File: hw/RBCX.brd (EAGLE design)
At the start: 100 x 100 mm, 463 parts, among them IC1 AMS1117-3.3, IC10 INA180A4, IC11 INA180A4, IC12 MPU-6050, IC13 STM32F103VCT6, IC2 DRV8833PWP, IC3 INA180A4, IC4 INA180A4, IC5 DRV8833PWP, IC6 INA180A4, IC7 INA180A4, IC8 INA180A4, IC9 INA180A4, P1 M1, P2 M2, P3 M3, P4 M4, Q1 NCE20P45Q, Q10 2N7002, Q2 NCE20P45Q, Q3 2N7002, Q4 2N7002, Q5 2N7002, Q6 2N7002, Q7 2N7002, Q8 2N7002, Q9 2N7002, X1 POWER_IN, X2 POWER_OUT, X3 52559-3092, X4 uUSB, Y1 5032/2P, Y2 3215_2P

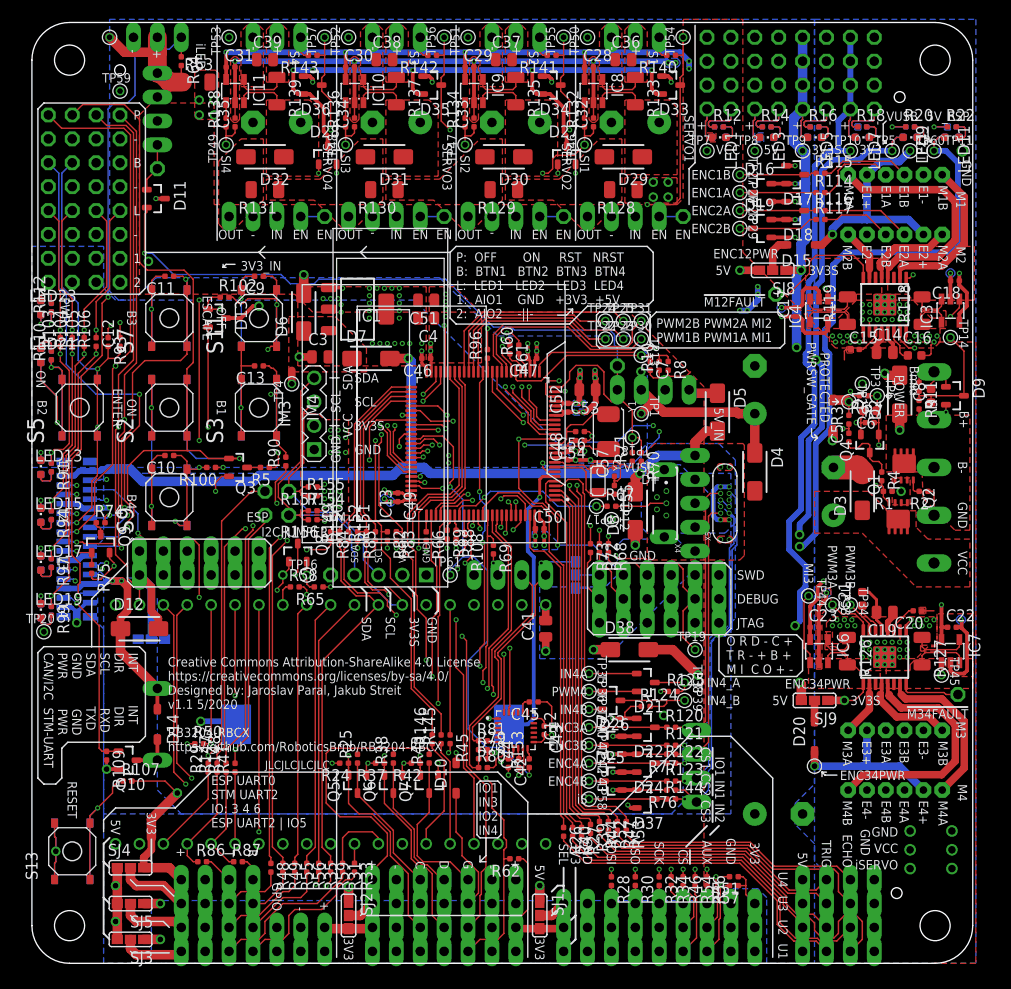
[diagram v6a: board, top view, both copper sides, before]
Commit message: hw: update and fix silkscreens
- fix position of labels
- add testpoint labels
- improve groups of text (separate columns in text labels)
- add label for capacitors polarity
- change layer from `tDocu` to `Document` for label in library `switch-omron.lbr`
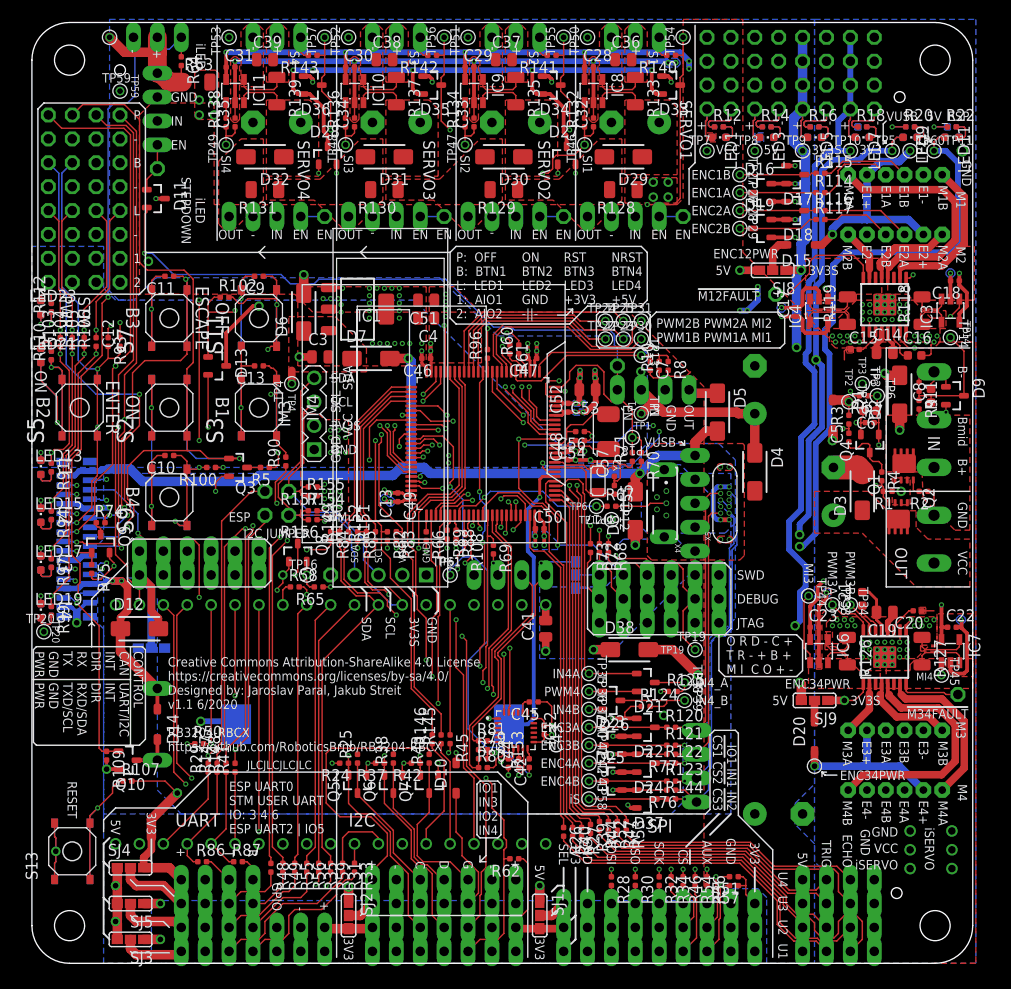
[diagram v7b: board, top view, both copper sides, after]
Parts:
- moved D13 5.08 mm to (19.7, 63.5)
- moved SJ7 0.95 mm to (12.7, 33.5)
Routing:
- net ESP_EN: track 177.6 -> 172.5 mm
- net BUTTON_OFF: track 33.1 -> 38.1 mm
- net +3V3S: track 567.6 -> 571.8 mm
- net EXPANDER_COM_PWR: track 30.0 -> 30.9 mm
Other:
- board text added: "BUZ"
- board text added: "CC1"
- board text added: "CC2"
- board text added: "CONTROL CAN INT DIR RX TX GND PWR"
- board text added: "Creative Commons Attribution-ShareAlike 4.0 License https://creativecommons.org/licenses/by-sa/4.0/ Designed by: Jaroslav Paral, Jakub Streit v1.1 6/2020 RB3204-RBCX https://github.com/RoboticsBrno/RB3204-RBCX"
- board text added: "DM"
- board text added: "ESP UART0 STM USER UART IO: 3 4 6 ESP UART2 | IO5"
- board text added: "ESP UART0 STM USER UART IO: 6 4 3 IO5 | ESP UART2"
- board text added: "MAIN POWERSUPPLY"
- board text added: "MI4"
- board text added: "NRST BTN4 LED4 +5V"
- board text added: "OFF BTN1 LED1 AIO1 AIO2"
- board text added: "ON BTN2 LED2 GND -||-"
- board text added: "ON BTN2 LED2 GND GND"
- board text added: "P: NRST B: BTN4 L: LED4 1: +5V 2: +5V"
- board text added: "P: OFF B: BTN1 L: LED1 1: AIO1 2: AIO2"
- board text added: "RB3204-RBCX v1.1 6/2020 CC-SA 4.0 https://github.com/ RoboticsBrno/ RB3204-RBCX"
- board text added: "RST BTN3 LED3 +3V3"
- board text added: "RST BTN3 LED3 +3V3 +3V3"
- board text added: "SBU1"
- board text added: "SBU2"
- board text added: "STM PWR"
- board text added: "TP1"
- board text added: "TP12"
- board text added: "TP13(V_BAT)"
- board text added: "TP14"
- board text added: "TP16"
- board text added: "TP18"
- board text added: "TP19"
- board text added: "TP2"
- board text added: "TP20"
- board text added: "TP3"
- board text added: "TP4"
- board text added: "TP59"
- board text added: "TP6"
- board text added: "TP61"
- board text added: "UART /I2C INT DIR RXD /SDA TXD /SCL GND PWR"
- board text added: "UART/I2C INT DIR RXD/SDA TXD/SCL GND PWR"
- board text added: "V_BAT/2"
- board text added: "iLED STEPDOWN"
- board text removed: "3V3_IN"
- board text removed: "5V_IN"
- board text removed: "CAN/I2C STM-UART PWR PWR GND GND SDA TXD SCL RXD DIR DIR INT INT"
- board text removed: "Creative Commons Attribution-ShareAlike 4.0 License https://creativecommons.org/licenses/by-sa/4.0/ Designed by: Jaroslav Paral, Jakub Streit v1.1 5/2020 RB3204-RBCX https://github.com/RoboticsBrno/RB3204-RBCX"
- board text removed: "D+"
- board text removed: "D-"
- board text removed: "ESP UART0 STM UART2 IO: 3 4 6 ESP UART2 | IO5"
- board text removed: "ESP UART0 STM UART2 IO: 6 4 3 IO5 | ESP UART2"
- board text removed: "INT INT DIR DIR SCL RXD SDA TXD GND GND PWR PWR CAN/I2C STM-UART"
- board text removed: "P: NRST RST ON OFF B: BTN4 BTN3 BTN2 BTN1 L: LED4 LED3 LED2 LED1 1: +5V +3V3 GND AIO1 2: +5V +3V3 GND AIO2"
- board text removed: "P: OFF ON RST NRST B: BTN1 BTN2 BTN3 BTN4 L: LED1 LED2 LED3 LED4 1: AIO1 GND +3V3 +5V 2: AIO2 -||-"
- board text removed: "POWER"
- board text removed: "PROTECTED"
- board text removed: "PWR"
- board text removed: "PWRSW_GATE"
- board text removed: "RB3204-RBCX v1.1 5/2020 https://github.com/ RoboticsBrno/RB3204-RBCX CC-SA 4.0"

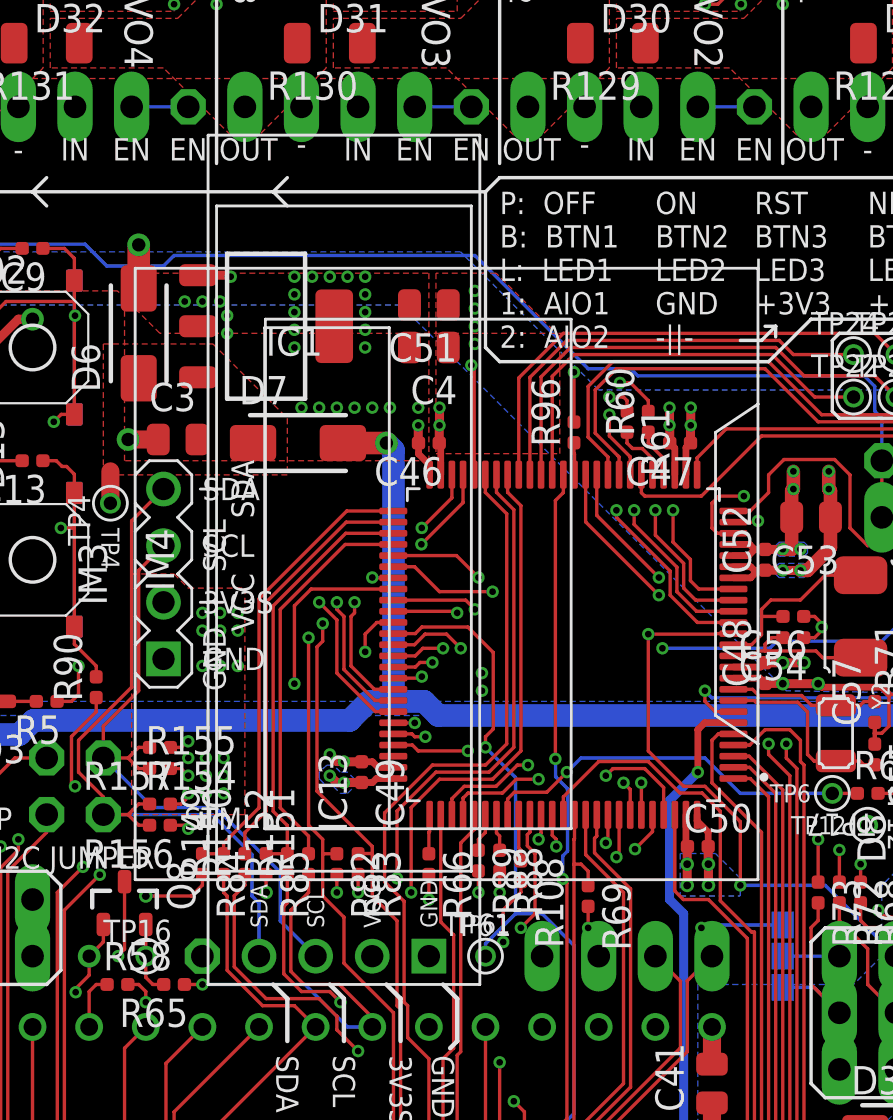
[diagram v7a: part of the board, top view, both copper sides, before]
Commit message: hw: change outline layer of display modules
- `diy-modules.lbr` - change outline layer from `tPlace` to `Document`
  - footprint `DISPLAY-OLED-128X32`
  - footprint `DISPLAY-OLED-128X64-I2C_W-HOLES`
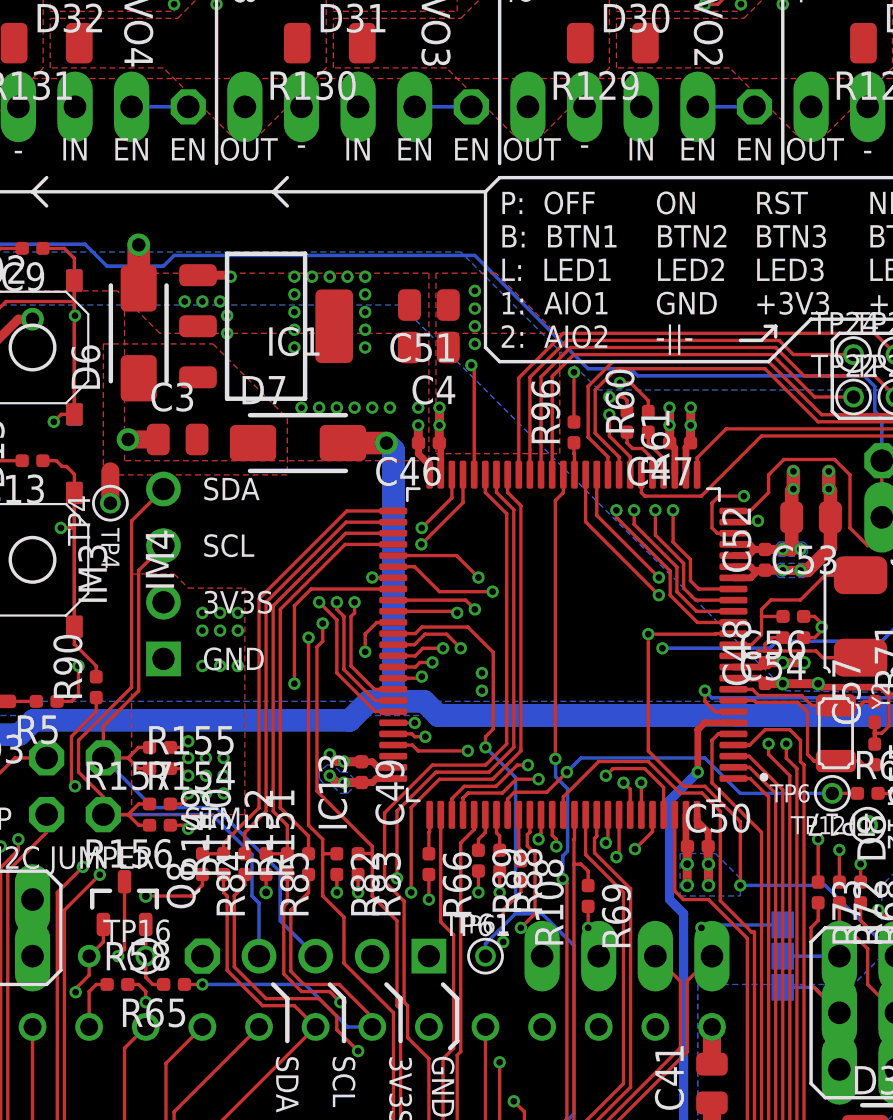
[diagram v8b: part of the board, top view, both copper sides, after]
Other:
- board text added: "D-"
- board text removed: "DM"
